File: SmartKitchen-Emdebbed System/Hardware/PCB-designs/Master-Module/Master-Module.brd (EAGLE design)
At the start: 160 x 100 mm, 9 parts, among them IC2 7805DT, J1 RJ11-2L-B, J2 RJ11-2L-B, J3 RJ11-2L-B

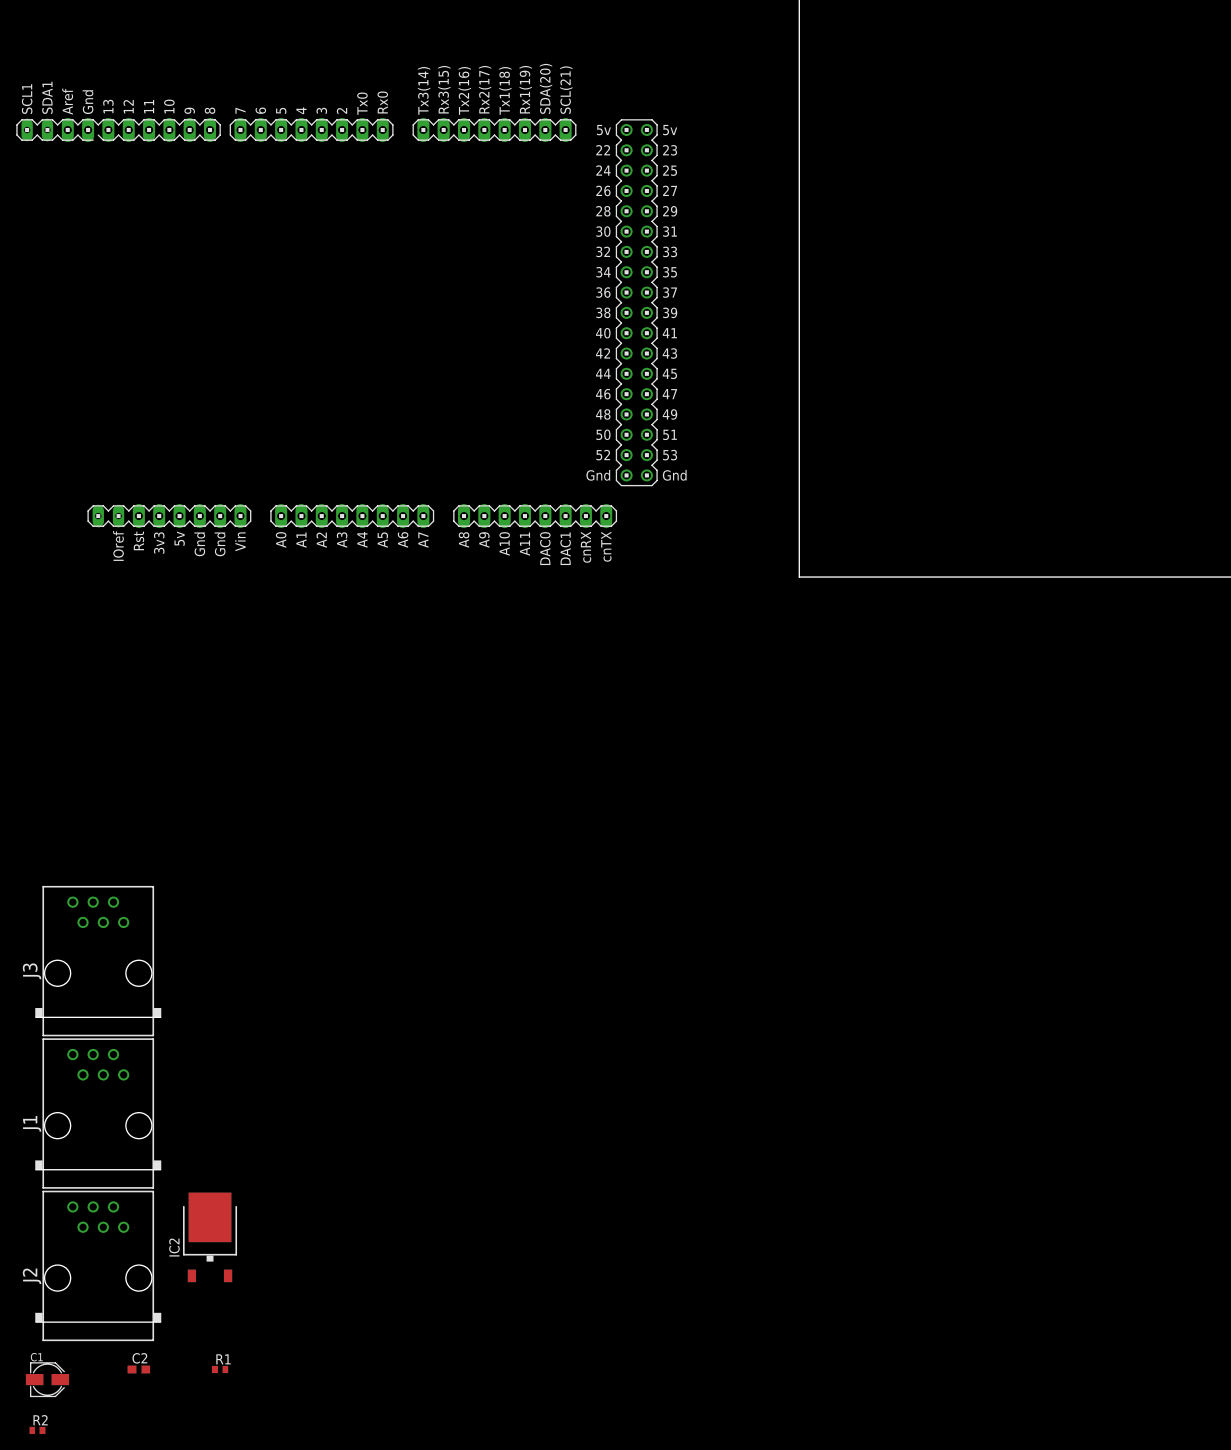
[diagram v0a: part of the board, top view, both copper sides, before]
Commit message: customizing components
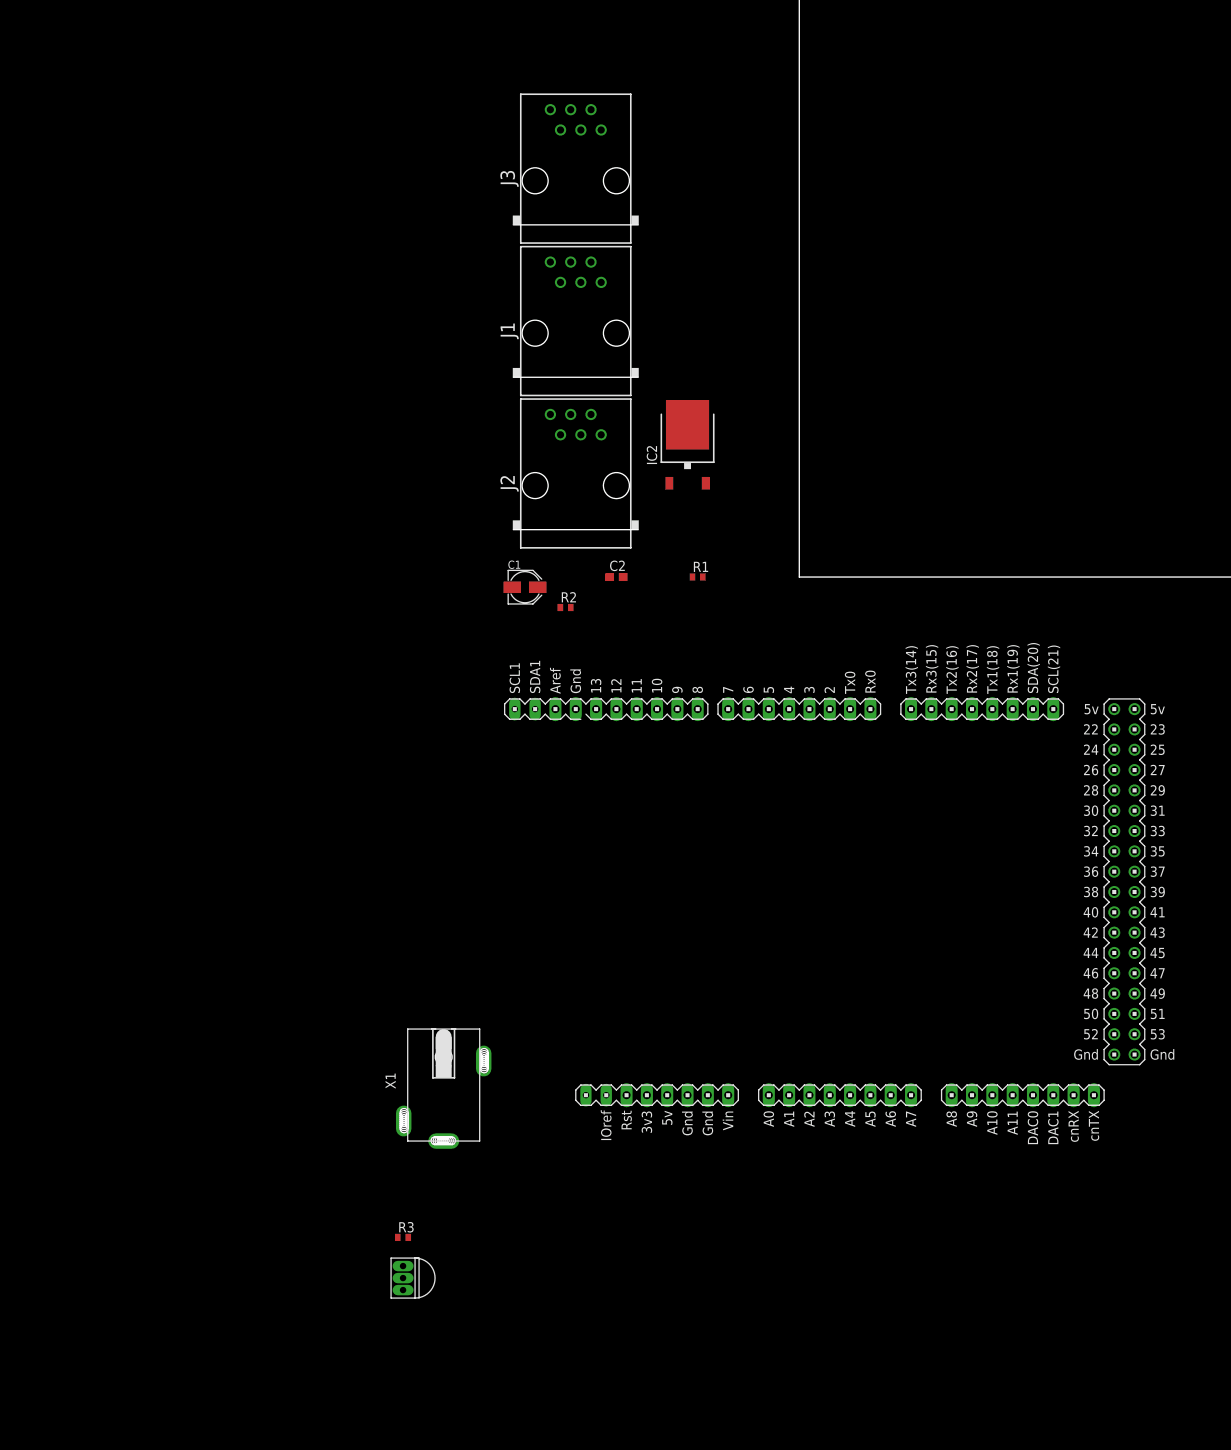
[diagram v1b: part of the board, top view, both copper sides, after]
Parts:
- added R3: 2k2, rcl:R0402
- added U$2: LM335, LM335:LM335
- added X1: K375M, con-power c:K375M
- moved R2 122.2 mm to (-29.2, -3.81)
- moved C1 115.7 mm to (-34.3, -1.27)
- moved C2 115.7 mm to (-22.9, 0.00)
- moved IC2 115.7 mm to (-14.0, 16.5)
- moved J1 115.7 mm to (-27.9, 30.5)
- moved J2 115.7 mm to (-27.9, 11.4)
- moved J3 115.7 mm to (-27.9, 49.5)
- moved R1 115.7 mm to (-12.7, 0.00)
- moved U$1 94.6 mm to (5.08, -39.4)
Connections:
- new net N$5: R3.1, U$1.A0, U$2.P$2
- net AGND: now also U$1.GND_1, U$1.GND_2, U$2.P$3, X1.P$1, X1.P$6
- net N$1: now also U$1.SDA
- net N$10: now also X1.P$7
- net N$2: now also U$1.RX0
- net N$21: now also R3.2, U$1.5V
- net N$3: now also U$1.SCL

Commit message: PCB shield
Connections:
- new net N$6: J3.3, U$1.7
- net AGND: now also J3.4, J3.5
- net N$21: now also J3.1
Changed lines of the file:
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@@
 <contactref element="U$1" pad="5V"/>
 <contactref element="R3" pad="2"/>
+<contactref element="J3" pad="1"/>
 <wire x1="-16.51" y1="-64.77" x2="-48.88" y2="-82.55" width="0" layer="19" extent="1-1"/>
 <wire x1="-28.56" y1="-3.81" x2="-16.51" y2="-64.77" width="0" layer="19" extent="1-1"/>
@@
 <wire x1="-12.05" y1="0" x2="-22.01" y2="0" width="0" layer="19" extent="1-1"/>
 <wire x1="-11.69" y1="11.71" x2="-12.05" y2="0" width="0" layer="19" extent="1-1"/>
+<wire x1="-31.115" y1="58.42" x2="-11.69" y2="11.71" width="0" layer="19" extent="1-1"/>
 </signal>
 <signal name="N$2">
@@
 <contactref element="U$1" pad="GND_2"/>
 <contactref element="U$2" pad="P$3"/>
+<contactref element="J3" pad="4"/>
+<contactref element="J3" pad="5"/>
 <wire x1="-49.45" y1="-68" x2="-49.53" y2="-89.13" width="0" layer="19" extent="1-1"/>
 <wire x1="-39.45" y1="-60.5" x2="-49.45" y2="-68" width="0" layer="19" extent="1-1"/>
@@
 <wire x1="-13.97" y1="19.01" x2="-29.845" y2="17.78" width="0" layer="19" extent="1-1"/>
 <wire x1="-29.845" y1="36.83" x2="-29.845" y2="17.78" width="0" layer="19" extent="1-1"/>
+<wire x1="-27.305" y1="55.88" x2="-29.845" y2="36.83" width="0" layer="19" extent="1-1"/>
+<wire x1="-26.035" y1="58.42" x2="-27.305" y2="55.88" width="0" layer="19" extent="1-1"/>
 </signal>
 <signal name="N$5">
@@
 <wire x1="-3.81" y1="-64.77" x2="-50.18" y2="-82.55" width="0" layer="19" extent="1-1"/>
 </signal>
+<signal name="N$6">
+<contactref element="J3" pad="3"/>
+<contactref element="U$1" pad="7"/>
+<wire x1="-8.89" y1="-16.51" x2="-28.575" y2="58.42" width="0" layer="19" extent="1-1"/>
+</signal>
 </signals>

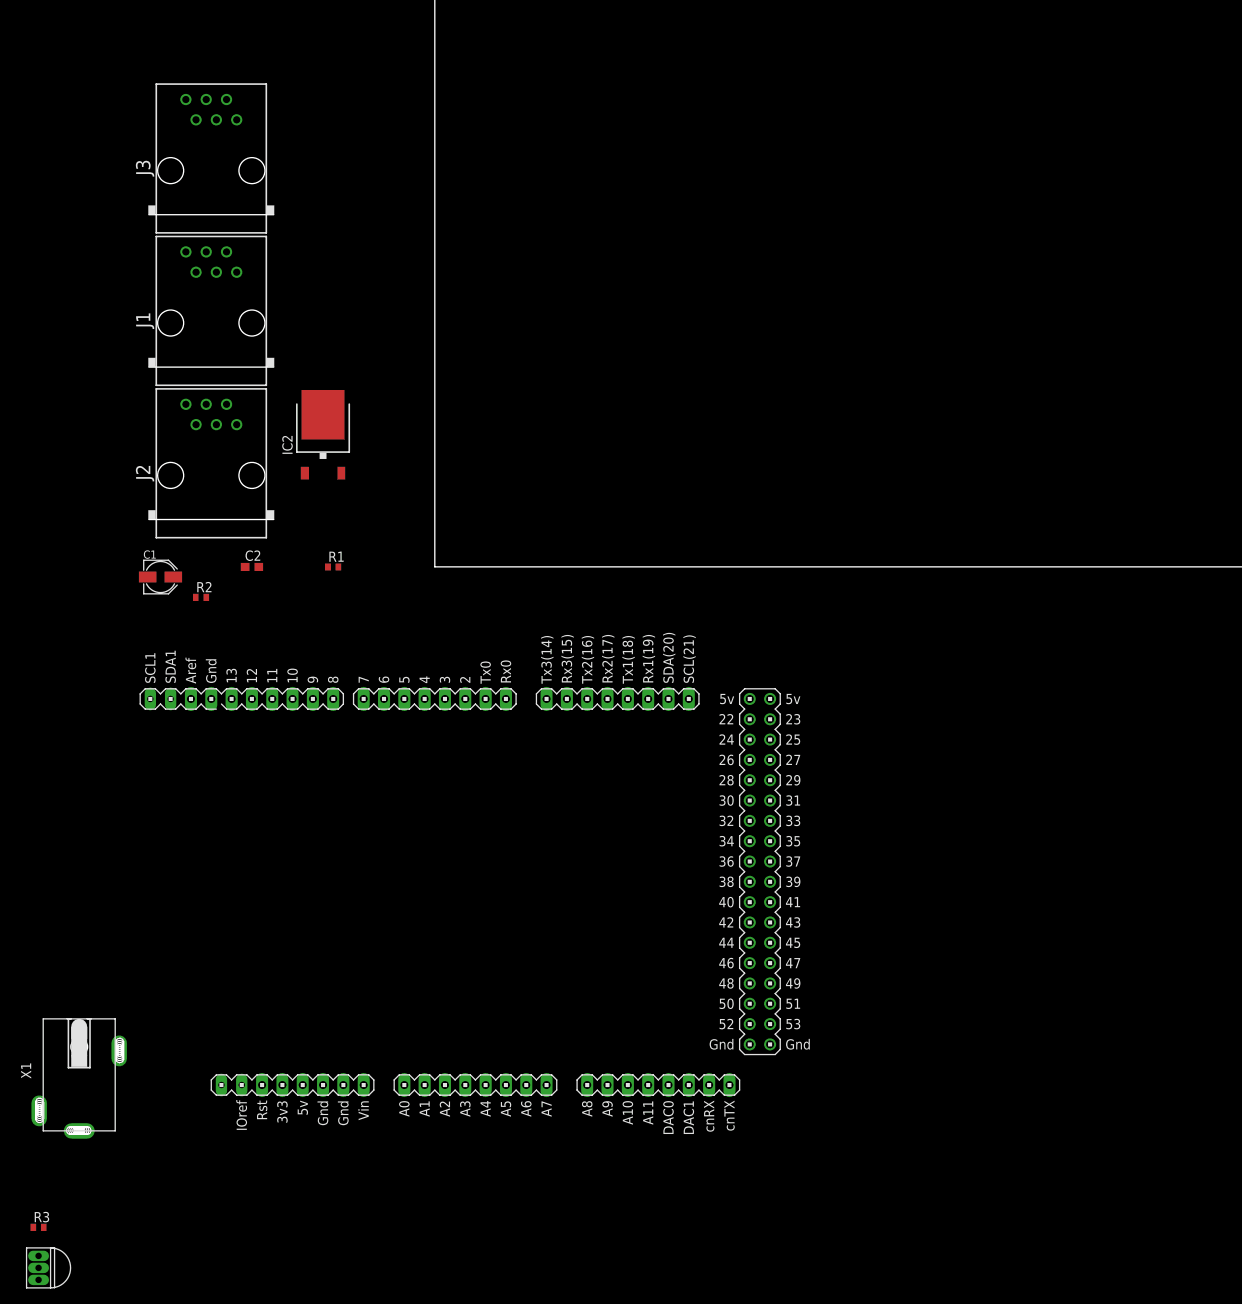
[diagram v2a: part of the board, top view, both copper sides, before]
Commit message: Adding stupid level-converter for serial connection
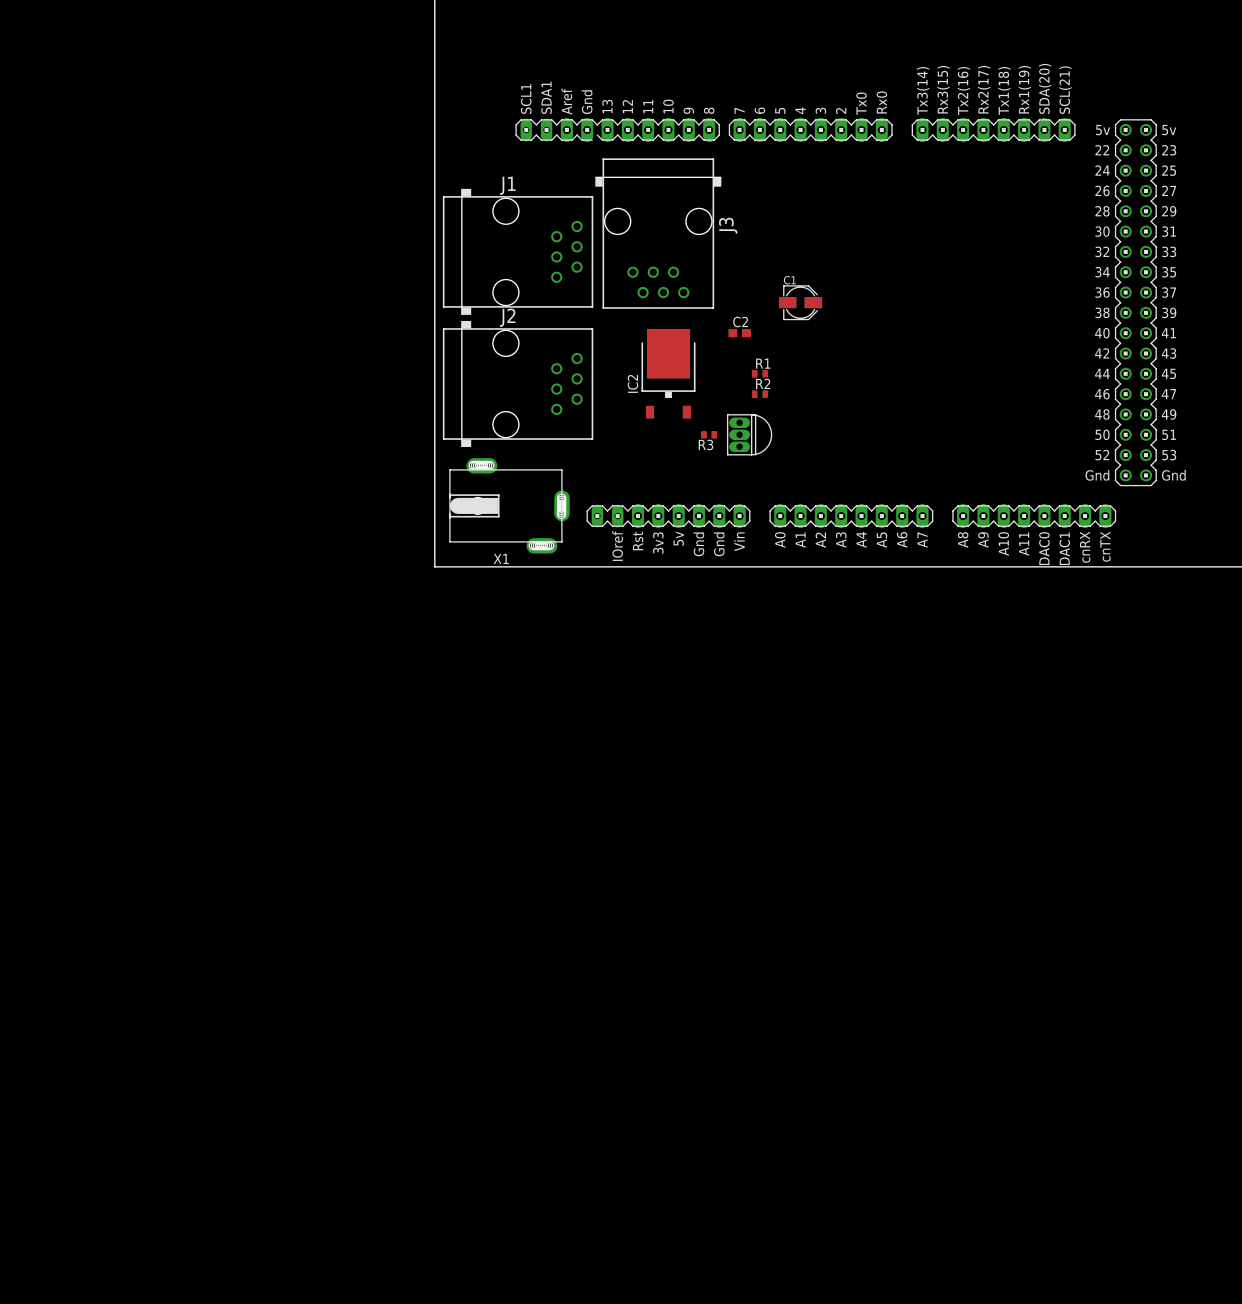
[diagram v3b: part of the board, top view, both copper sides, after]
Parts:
- moved U$2 136.1 mm to (38.1, 16.5)
- moved R3 129.8 mm to (34.3, 16.5), turned to 180 degrees
- moved X1 88.9 mm to (8.89, 7.62), turned to 90 degrees
- moved C1 87.0 mm to (45.7, 33.0)
- moved U$1 85.2 mm to (52.1, 31.8)
- moved R2 74.3 mm to (40.6, 21.6)
- moved C2 67.6 mm to (38.1, 29.2)
- moved R1 58.5 mm to (40.6, 24.1)
- moved J3 56.2 mm to (27.9, 43.2), turned to 180 degrees
- moved IC2 43.8 mm to (29.2, 24.1)
- moved J2 38.6 mm to (8.89, 22.9), turned to 270 degrees
- moved J1 37.9 mm to (8.89, 39.4), turned to 270 degrees
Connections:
- removed net N$21: C2.2, IC2.2, J3.1, R1.2, R2.2, R3.2, U$1.5V
- new net N$4: C2.2, IC2.2, J3.1, R1.2, R2.2, R3.2
- net N$10: now also U$1.VIN
